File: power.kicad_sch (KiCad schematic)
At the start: 76 parts, among them J1 PWR + CAN harness, Q1 IPD068N10, Q2 AO3401A, Q3 2N7002, U1 LM74700-Q1, U2 TLV431A, U3 LM5164 (5V), U4 LM5164 (3V3)

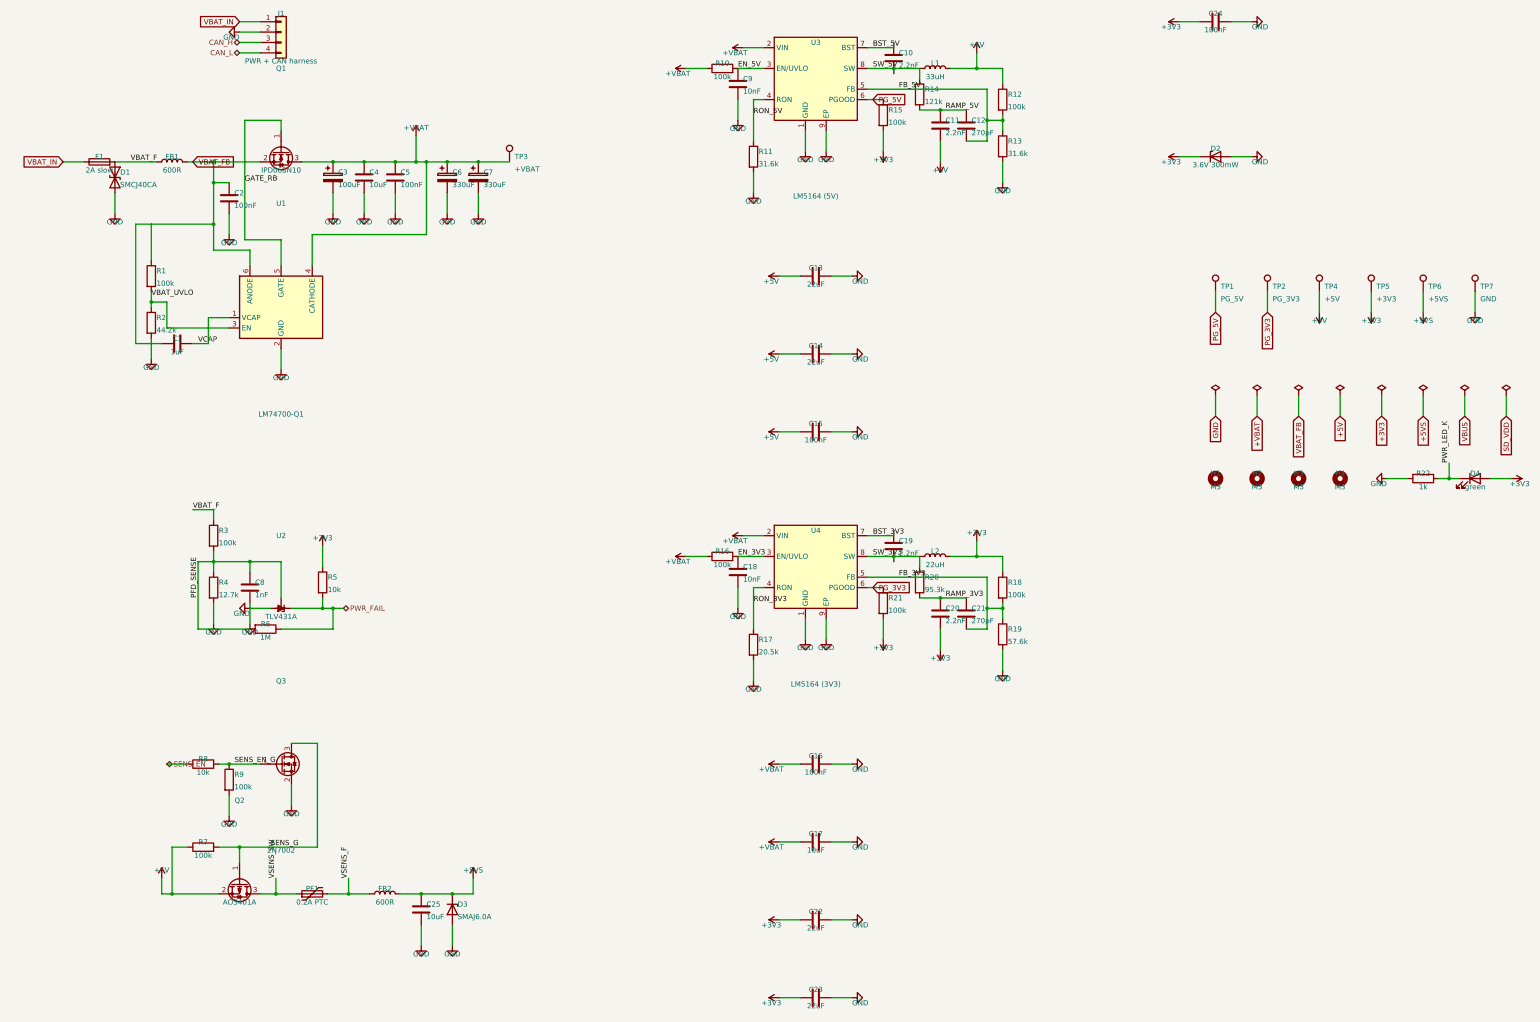
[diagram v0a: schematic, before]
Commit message: Re-scope the fork as a carrier board: no power section, differential analog, K-line
The shield idea does not survive measurement. Component courtyard on the
parent is 3052 mm2 over an 84 x 100 board -- 36% packing, not the 50% I had
been estimating -- and a DevKitC-1 is 63 x 25.5 = 1607 mm2. The parts alone
were 1.4x the whole dev board. So this is a carrier the dev board plugs into,
not a shield that fits on top of one.

Power section deleted entirely. It was 1746 mm2, 57% of the board, for two
rails the DevKitC-1 already makes from its USB-C. Gone: both LM5164 bucks and
everything around them, the LM74700 ideal diode, the reverse-battery FET, the
three electrolytic cans, the 12 V input, and the sensor-rail load switch.
Both rails are now inputs, taken up through the sockets -- which reverses the
earlier "feed 5 V only" rule, because there is no longer a second regulator
to parallel against.

Hold-up is a supercapacitor, not electrolytics. The first sizing was wrong:
energy goes as V-squared and the usable window at 5 V is 4.2 -> 3.6 V, so
2000 uF buys 12.5 ms, not the ~50 ms claimed. 0.5 F over the same window is
2.5 s, in less area than one of the 100 V cans it replaces. Low-ESR
cylindrical cells specifically -- coin EDLCs are 30-200 ohm and cannot source
120 mA at all.

Analog runs differentially. The board is grounded twice now, through the
sensor loom and through USB by way of a charger elsewhere in the car, and a
few hundred mV of chassis drop is 6% of a 0-5 V channel -- which makes the
0.1% dividers pointless. The correction has to be at the divider, not the
ADC, so the sensor ground comes back as a Kelvin wire through a matched
attenuator. Two ADS1115s, because one MUX only offers three channels against
a shared negative.

K-line added, discrete rather than an L9637D: that part's TXD threshold is
0.7*VCC = 3.5 V and a 3.3 V GPIO cannot meet it. Low-side 2N7002, clamped
22k/10k receiver, optional ISO 9141 tester pull-up on a jumper.

Pin map regrouped by boa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
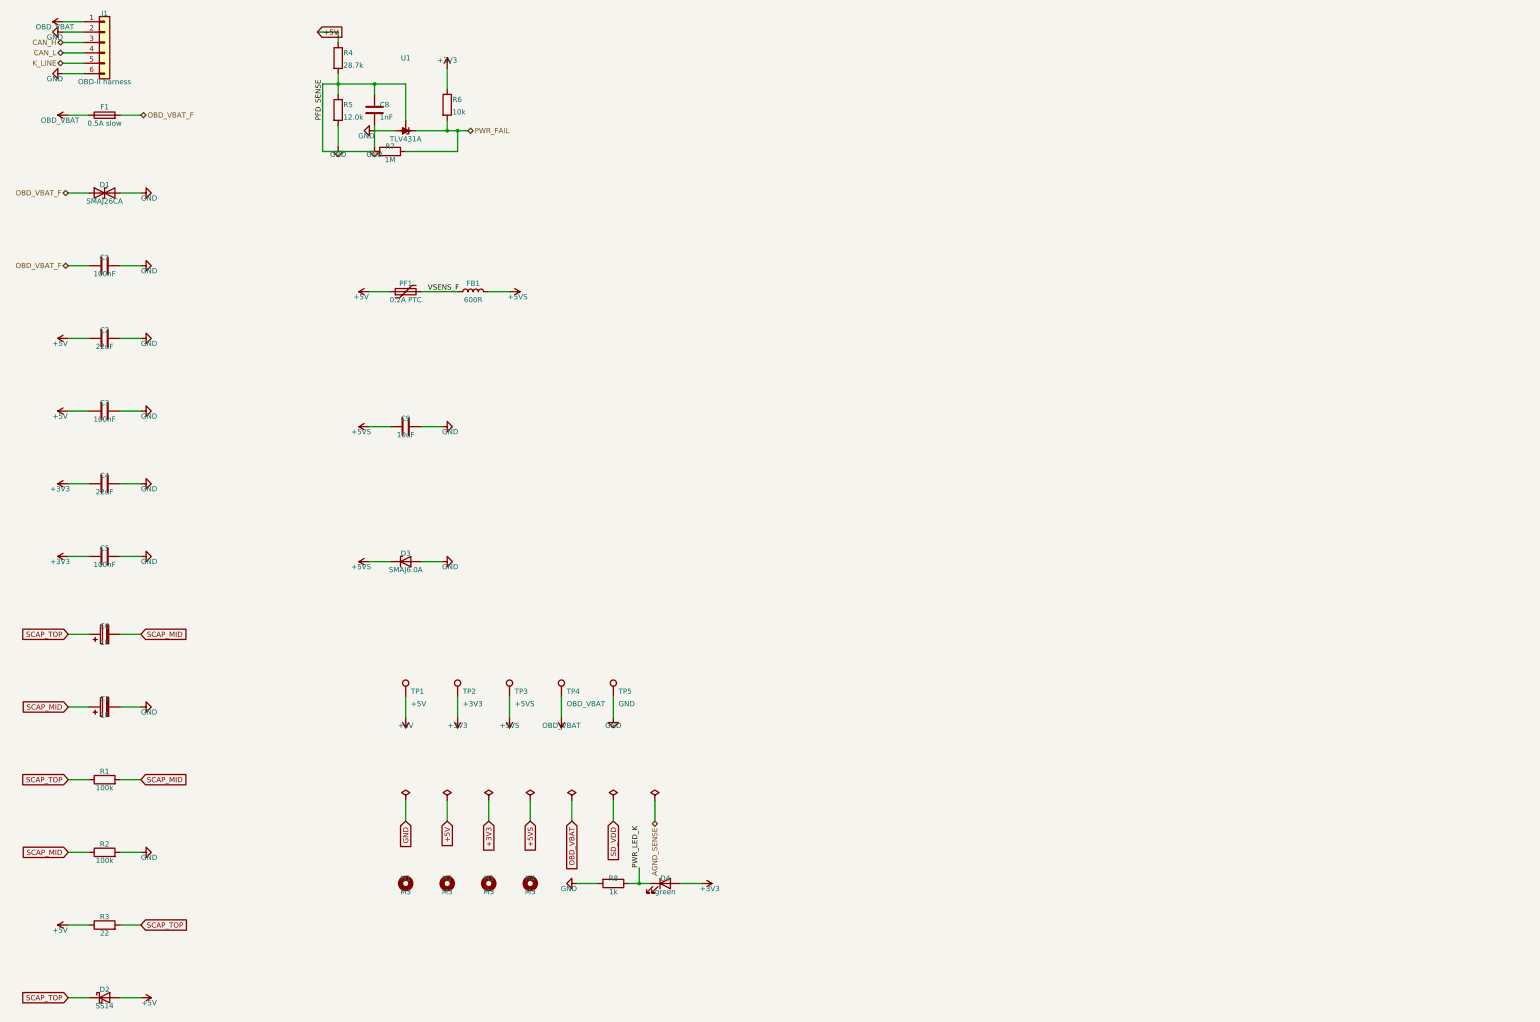
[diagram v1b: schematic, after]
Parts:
- removed C10, C11, C19, C20: 2.2nF, Capacitor_SMD:C_0805_2012Metric, symbol Device:C
- removed C12, C21: 270pF, Capacitor_SMD:C_0805_2012Metric, symbol Device:C
- removed C13, C14, C22, C23: 22uF, Capacitor_SMD:C_1206_3216Metric, symbol Device:C
- removed C15, C16, C24: 100nF, Capacitor_SMD:C_0805_2012Metric, symbol Device:C
- removed C17, C25: 10uF, Capacitor_SMD:C_1206_3216Metric, symbol Device:C
- removed C18: 10nF, Capacitor_SMD:C_0805_2012Metric, symbol Device:C
- removed FB2: 600R, Inductor_SMD:L_0805_2012Metric, symbol Device:L
- removed L1: 33uH, Inductor_SMD:L_Sunlord_SWPA8040S, symbol Device:L
- removed L2: 22uH, Inductor_SMD:L_Sunlord_SWPA8040S, symbol Device:L
- removed Q1: IPD068N10, Package_TO_SOT_SMD:TO-252-3_TabPin2, symbol Transistor_FET:Q_NMOS_GSD
- removed Q2: AO3401A, Package_TO_SOT_SMD:SOT-23, symbol Transistor_FET:Q_PMOS_GSD
- removed Q3: 2N7002, Package_TO_SOT_SMD:SOT-23, symbol Transistor_FET:Q_NMOS_GSD
- removed R10, R12, R15, R16, R18, R21, R9: 100k, Resistor_SMD:R_0805_2012Metric, symbol Device:R
- removed R11, R13: 31.6k, Resistor_SMD:R_0805_2012Metric, symbol Device:R
- removed R14: 121k, Resistor_SMD:R_0805_2012Metric, symbol Device:R
- removed R17: 20.5k, Resistor_SMD:R_0805_2012Metric, symbol Device:R
- removed R19: 57.6k, Resistor_SMD:R_0805_2012Metric, symbol Device:R
- removed R20: 95.3k, Resistor_SMD:R_0805_2012Metric, symbol Device:R
- removed R22: 1k, Resistor_SMD:R_0805_2012Metric, symbol Device:R
- removed TP6: +5VS, TestPoint:TestPoint_Pad_D1.5mm, symbol Connector:TestPoint
- removed TP7: GND, TestPoint:TestPoint_Pad_D1.5mm, symbol Connector:TestPoint
- removed U2: TLV431A, Package_TO_SOT_SMD:SOT-23, symbol Reference_Voltage:TL431DBZ
- removed U3: LM5164 (5V), Package_SO:SOIC-8-1EP_3.9x4.9mm_P1.27mm_EP2.95x4.9mm_Mask2.71x3.4mm_ThermalVias, symbol Regulator_Switching:LM5164DDA
- removed U4: LM5164 (3V3), Package_SO:SOIC-8-1EP_3.9x4.9mm_P1.27mm_EP2.95x4.9mm_Mask2.71x3.4mm_ThermalVias, symbol Regulator_Switching:LM5164DDA
- C1: value 1uF -> 100nF; Note LM74700 charge-pump reservoir -> (none); Voltage 50V -> 100V
- C2: value 100nF -> 22uF; footprint Capacitor_SMD:C_0805_2012Metric -> Capacitor_SMD:C_1206_3216Metric; Note LM74700 ANODE input capacitor: the datasheet requires a min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 -> Bulk at the 5 V socket pin; Voltage 100V -> 16V
- C3: value 100uF -> 100nF; footprint Capacitor_SMD:CP_Elec_10x10.5 -> Capacitor_SMD:C_0805_2012Metric; symbol Device:C_Polarized -> Device:C; MPN Nichicon UCD2A101MNL1GS -> (none); Note Bulk hold-up; any 100uF >=80V SMD electrolytic on a 10x10.5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 -> (none); Voltage 100V -> 16V
- C4: value 10uF -> 22uF; Note Switcher input bypass -> Bulk at the 3V3 socket pin; Voltage 100V -> 16V
- C5: Note HF bypass -> (none); Voltage 100V -> 16V
- C6: value 330uF -> 1F; footprint Capacitor_SMD:CP_Elec_16x22 -> Capacitor_THT:CP_Radial_D8.0mm_P3.50mm; MPN (none) -> Eaton HB1030-2R5105-R; Note Power-fail ride-through. With the sensor rail shed and the 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 -> Hold-up cell 1 of 2 in series -> 0.5 F at 5.4 V. Anything f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; Voltage 100V -> 2.7V
- C7: value 330uF -> 1F; footprint Capacitor_SMD:CP_Elec_16x22 -> Capacitor_THT:CP_Radial_D8.0mm_P3.50mm; MPN (none) -> Eaton HB1030-2R5105-R; Note Power-fail ride-through. With the sensor rail shed and the 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 -> Hold-up cell 2 of 2 in series -> 0.5 F at 5.4 V. Anything f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; Voltage 100V -> 2.7V
- C8: Note Just enough to keep switching noise off the reference. Larg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 -> Keeps switching noise off the reference
- C9: value 10nF -> 10uF; footprint Capacitor_SMD:C_0805_2012Metric -> Capacitor_SMD:C_1206_3216Metric; Note EN sits on a bare 100k to VBAT; this keeps a high-impedance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 -> (none); Voltage 100V -> 16V
- D1: value SMCJ40CA -> SMAJ26CA; footprint Diode_SMD:D_SMC -> Diode_SMD:D_SMA; MPN Littelfuse SMCJ40CA -> Diodes Inc SMAJ26CA-13-F; Note 40V standoff / 64.5V clamp @ 1500W, bidirectional: absorbs 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 -> Clamps the OBD 12 V node. 400 W is enough here, not the par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
- D2: value 3.6V 300mW -> SS14; footprint Diode_SMD:D_SOD-323 -> Diode_SMD:D_SMA; symbol Device:D_Zener -> Device:D_Schottky; MPN onsemi MM3Z3V6T1G -> SS14; Note Rail clamp: an analog input shorted to battery back-feeds ~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 -> Discharge path, bypassing the charge resistor. Anode on the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
- D4: Note The board's only LED: +3V3 is up, so the whole supply chain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 -> Shield 3V3 is up, which means the dev board is in its socke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
- F1: value 2A slow -> 0.5A slow; MPN Littelfuse 0466002.NR -> Littelfuse 0466.500NR; Note Sacrificial: only opens on a hard fault, not on reverse pol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 -> Protects the optional K-line pull-up only. The battery-sens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
- FB1: footprint Inductor_SMD:L_1206_3216Metric -> Inductor_SMD:L_0805_2012Metric; MPN Wurth 742792625 -> Wurth 742792022; Note Conducted-emissions bead -> (none)
- J1: value PWR + CAN harness -> OBD-II harness; footprint Connector_JST:JST_PH_B4B-PH-K_1x04_P2.00mm_Vertical -> Connector_JST:JST_PH_B6B-PH-K_1x06_P2.00mm_Vertical; symbol Connector_Generic:Conn_01x04 -> Connector_Generic:Conn_01x06; MPN JST B4B-PH-K-S(LF)(SN) -> JST B6B-PH-K-S(LF)(SN); Note Pin 1 +12V, 2 GND, 3 CAN_H, 4 CAN_L (Autosport Labs harness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 -> OBD-II pins 16/4/6/14/7/5. Pin 1 is sense only -- the board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
- PF1: Note Resettable: a shorted sensor wire trips this, not the board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 -> Resettable: a shorted sensor wire trips this, not the dev b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
- R1: Note UVLO upper leg -> Cell balancing, upper
- R2: value 44.2k -> 100k; Note UVLO lower leg. Ratio 0.3065 against V_EN_IH 1.06/2.0/2.6V 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 -> Cell balancing, lower
- R3: value 100k -> 22; footprint Resistor_SMD:R_0805_2012Metric -> Resistor_SMD:R_1206_3216Metric; Note Power-fail divider, upper leg -> Inrush limit. 1206 for the pulse rating: 210 mA into 22 ohm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; Tolerance 1% -> (none)
- R4: value 12.7k -> 28.7k; Note Lower leg: trips at 1.24V * 112.7/12.7 = 11.00V on the harn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 -> Power-fail divider, upper leg
- R5: value 10k -> 12.0k; Note Cathode pull-up. 10k gives the part 330uA, over the TLV431'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 -> Lower leg: trips at 1.24V * 40.7/12.0 = 4.20V. The rail sit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; Tolerance (none) -> 1%
- R6: value 1M -> 10k; Note Hysteresis, about 0.3V at the harness. Without it a battery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 -> Cathode pull-up. 10k gives the part 330uA, over the TLV431'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
- R7: value 100k -> 1M; Note Holds the switch off when nothing drives it -> Hysteresis, about 0.1 V at the rail. A USB rail is noisier 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
- R8: value 10k -> 1k; Note GPIO series/gate resistor -> (none)
- TP1: value PG_5V -> +5V
- TP2: value PG_3V3 -> +3V3
- TP3: value +VBAT -> +5VS
- TP4: value +5V -> OBD_VBAT
- TP5: value +3V3 -> GND
- U1: value LM74700-Q1 -> TLV431A; footprint Package_TO_SOT_SMD:SOT-23-6 -> Package_TO_SOT_SMD:SOT-23; symbol Power_Management:LM74700 -> Reference_Voltage:TL431DBZ; MPN LM74700QDBVRQ1 -> TLV431ASN1T1G; Note Ideal-diode controller; blocks reverse battery via Q1 -> Power-fail comparator. Below the trip point it stops conduc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
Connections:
- net EN_5V is gone; now on net +5VS: C9.1
- net PG_3V3 is gone; now on net +3V3: TP2.1
- net PG_5V is gone; now on net +5V: TP1.1
- net SENS_EN is gone; now on net PWR_LED_K: R8.1
- net SENS_EN_G is gone; now on net GND: R8.2
- net SENS_G is gone; now on net PFD_SENSE: R7.2
- net VSENS_SW is gone; now on net +5V: PF1.1
- net +3V3: now also C4.1, C5.1, R6.1; no longer D2.1 (K), R5.1, TP5.1
- net +5V: now also C2.1, C3.1, D2.2 (A), R3.1, R4.1; no longer R7.1, TP4.1
- net +5VS: now also FB1.2, TP3.1
- net GND: now also C1.2, J1.6 (Pin_6), R5.2, TP5.1, U1.3 (A); no longer C6.2, D2.2 (A), R4.2, U1.2 (GND)
- net PFD_SENSE: now also R4.2, R5.1, U1.2 (REF); no longer R3.2, R4.1, R6.2
- net PWR_FAIL: now also R6.2, R7.1, U1.1 (K); no longer R5.2, R6.1
- net VSENS_F: now also FB1.1
- removed net +VBAT: C3.1, C4.1, C5.1, C6.1, C7.1, TP3.1, U1.4 (CATHODE)
- removed net GATE_RB: U1.5 (GATE)
- net VBAT_F renamed OBD_VBAT_F
- net OBD_VBAT_F: now also C1.1; no longer FB1.1, R3.1
- removed net VBAT_FB: C1.2, C2.1, FB1.2, R1.1, U1.6 (ANODE)
- net VBAT_IN renamed OBD_VBAT
- net OBD_VBAT: now also TP4.1
- net VBAT_UVLO renamed SCAP_MID
- net SCAP_MID: now also C6.2, C7.1; no longer U1.3 (EN)
- removed net VCAP: C1.1, U1.1 (VCAP)
- new net K_LINE: J1.5 (Pin_5)
- new net SCAP_TOP: C6.1, D2.1 (K), R1.1, R3.2
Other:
- moved on the sheet: C1, C2, C4, C5, C6, C7, C8, C9, D1, D2, D3, D4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

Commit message: Second CAN bus, single analog range, and three placement bugs the render caught
TWO CAN BUSES AT ONCE NEEDS A SECOND CONTROLLER. The ESP32-S3 has exactly
one TWAI peripheral. Two transceivers on it would give a bus you can pick at
runtime through the GPIO matrix, never two live at once, and the point of a
second bus is watching the powertrain and the body bus together. So the
second channel is an MCP2518FD on SPI (SOIC-14, KiCad ships the pin-compatible
MCP2517FD symbol) with its own 40 MHz crystal, its own TJA1051 -- same part
as CAN 1, so two positions on one BOM line -- choke, split termination and
clamps.

That cost five pins against two spare. The three came from dropping the
microSD to 1-bit SDMMC, which measurement says is free: the busiest case this
logger will see is ~128 kB/s against 1-bit's ~1500 kB/s, and bus width does
not touch the card's internal write stall, which is the only thing the
hold-up budget is actually sized around. The card keeps its D1/D2/D3
pull-ups because a card samples DAT3 at power-up and drops into SPI mode if
it finds it low -- they simply stop at the socket now.

Jumpers on the aux harness pins pick K-line or the second CAN pair, because
those two genuinely cannot share a wire: K-line idles at battery voltage and
a CAN transceiver biases its bus to 2.5 V. The clamps sit ahead of the
jumpers so the protection is the same either way, which also let the K-line
drop its own TVS. Default is K-line, which is what an R53 wants.

ANALOG DOWN TO ONE RANGE. The bypass and range-select jumpers are gone --
twelve jumpers and four resistors -- and every channel is a fixed 2.21/13.21
divider spanning 0-16 V, so a 5 V and a 12 V sensor both fit without
touching anything. Resolution was never the reason for a narrower range: a
5 V sensor lands at 0.836 V, which on a 16-bit ADS1115 is 6688 counts.

The real reason is the differential ground. A channel switched to 0-16 V
while the shared return attenuator stayed at the 0-5 V ratio subtracts
0.5769*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
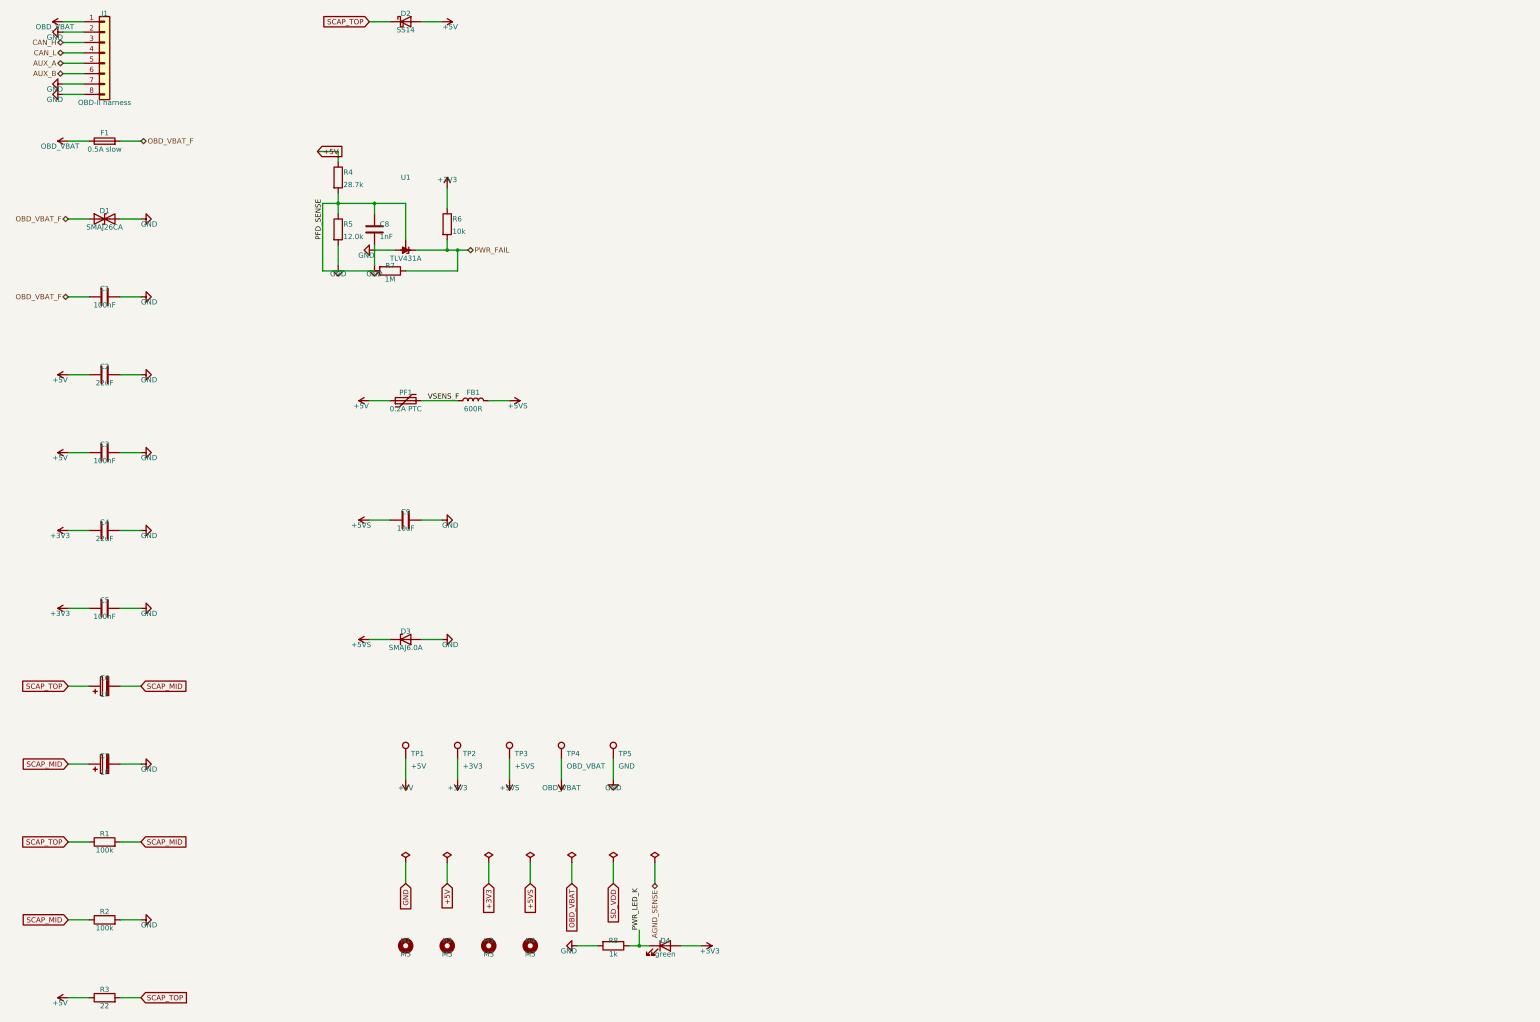
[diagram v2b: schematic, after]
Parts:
- J1: footprint Connector_JST:JST_PH_B6B-PH-K_1x06_P2.00mm_Vertical -> Connector_JST:JST_PH_B8B-PH-K_1x08_P2.00mm_Vertical; symbol Connector_Generic:Conn_01x06 -> Connector_Generic:Conn_01x08; MPN JST B6B-PH-K-S(LF)(SN) -> JST B8B-PH-K-S(LF)(SN); Note OBD-II pins 16/4/6/14/7/5. Pin 1 is sense only -- the board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 -> Pins 3/4 are the first CAN bus, always. Pins 5/6 are the se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
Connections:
- net GND: now also J1.7 (Pin_7), J1.8 (Pin_8); no longer J1.6 (Pin_6)
- net K_LINE renamed AUX_A
- new net AUX_B: J1.6 (Pin_6)
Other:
- moved on the sheet: C1, C2, C3, C4, C5, C6, C7, C8, C9, D1, D2, D3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
